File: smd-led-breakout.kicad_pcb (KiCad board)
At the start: 2 copper layers, 10 x 20 mm, 13 parts

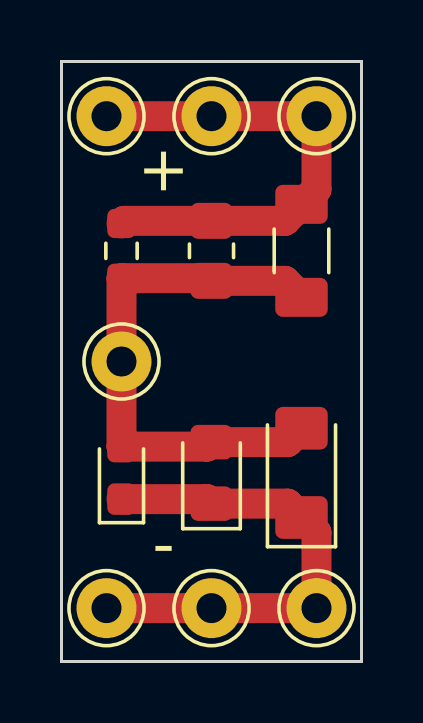
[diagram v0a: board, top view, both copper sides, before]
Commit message: Added bridge for measuring current.
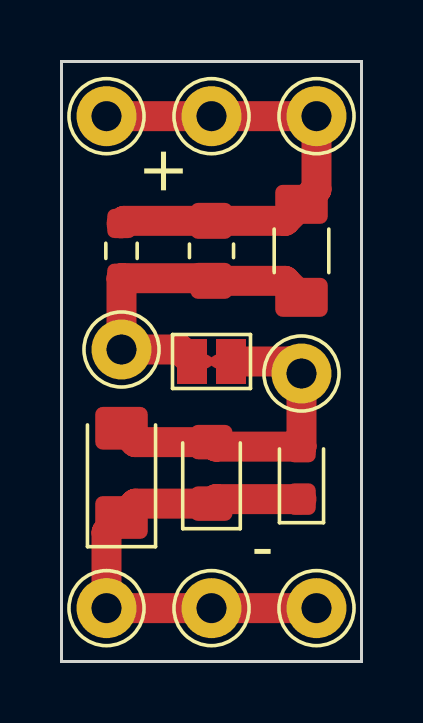
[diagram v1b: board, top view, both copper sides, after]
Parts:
- added JP1: SolderJumper_2_Bridged, _:SolderJumper-2_P1.3mm_Bridged_Pad1.0x1.5mm, F.Cu at (75.0, 75.0)
- added TP5: TestPoint, Connector_Pin:Pin_D1.0mm_L10.0mm, F.Cu at (78.0, 75.4)
- moved D1 6.00 mm to (78.0, 78.7)
- moved D3 6.00 mm to (72.0, 78.7)
- moved TP4 0.40 mm to (72.0, 74.6)
- renumbered TP5 to TP6, TP6 to TP7, TP7 to TP8
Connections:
- D1 pad 2: Net-(D2-Pad2) -> Net-(D1-Pad2)
- D2 pad 2: Net-(D2-Pad2) -> Net-(D1-Pad2)
- D3 pad 2: Net-(D2-Pad2) -> Net-(D1-Pad2)
- R1 pad 2: Net-(D2-Pad2) -> Net-(R1-Pad2)
- R2 pad 2: Net-(D2-Pad2) -> Net-(R1-Pad2)
- R3 pad 2: Net-(D2-Pad2) -> Net-(R1-Pad2)
- TP4 pad 1: Net-(D2-Pad2) -> Net-(R1-Pad2)
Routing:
- net Net-(D2-Pad2): track 18.1 -> 0.00 mm
- net Net-(D1-Pad2): track 0.00 -> 11.2 mm
- net Net-(R1-Pad2): track 0.00 -> 11.2 mm

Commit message: Refinements
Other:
- board text added: "smd-led-breakout 0.2a 10-May-23 mjd@afork.com"
